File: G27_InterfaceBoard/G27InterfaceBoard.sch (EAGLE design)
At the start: 24 parts, among them IC1 LMV321M5, J1 Pedal, J2 Shifter, J3 Steering, U1 LMV324

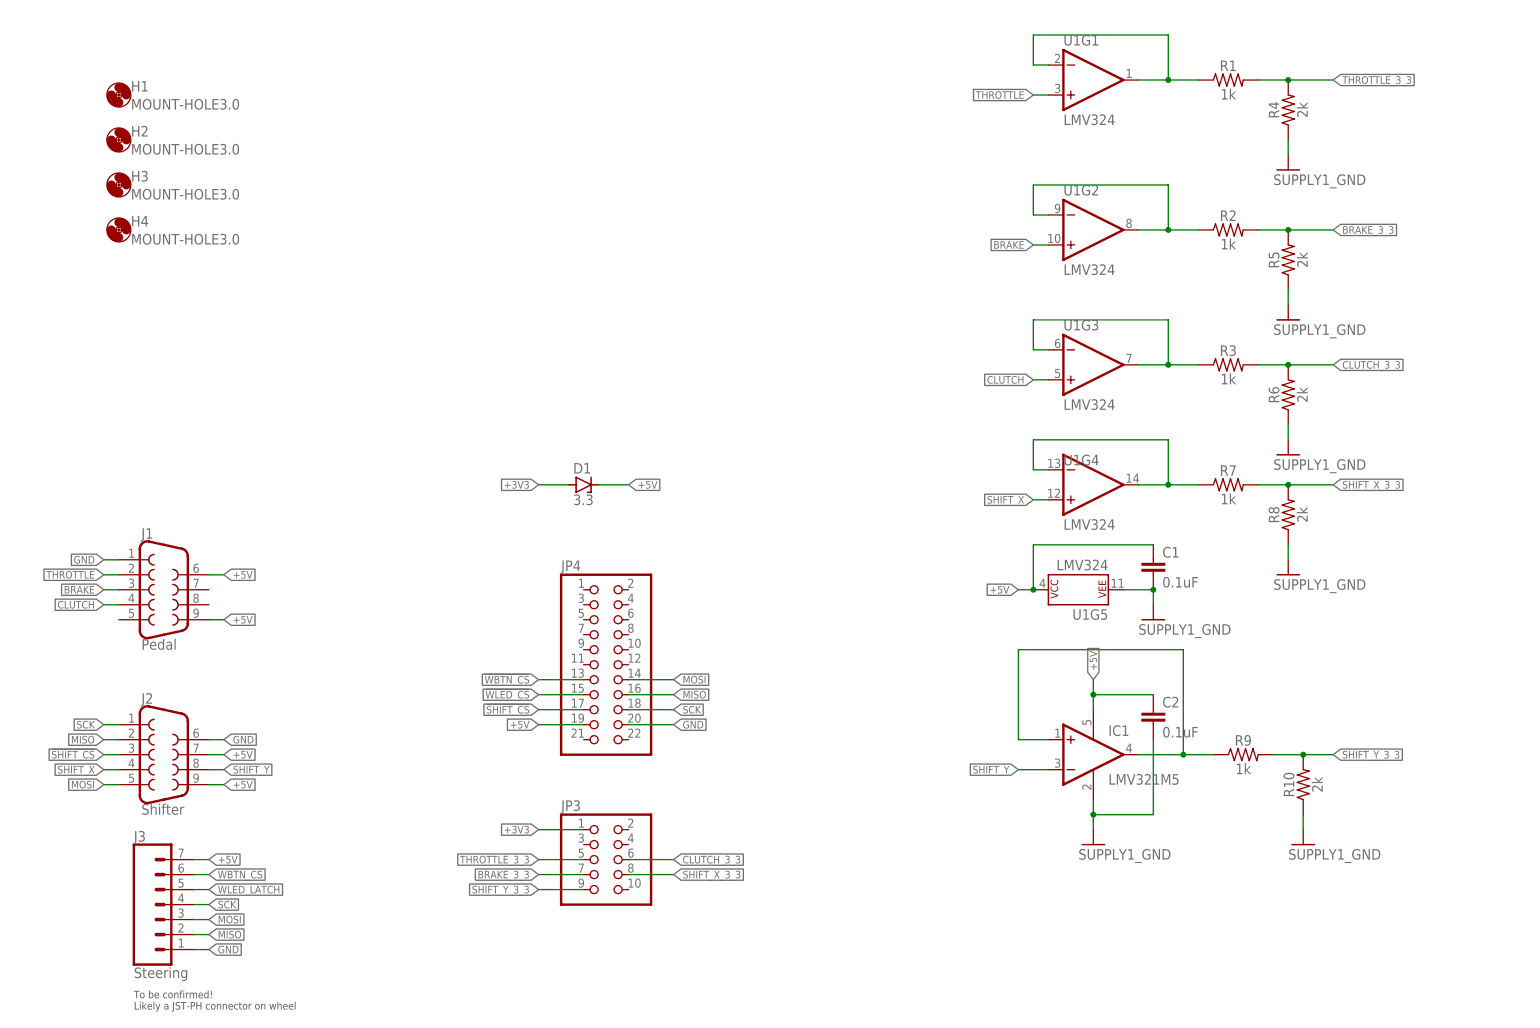
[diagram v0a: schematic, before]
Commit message: Modfications to board based on testing.
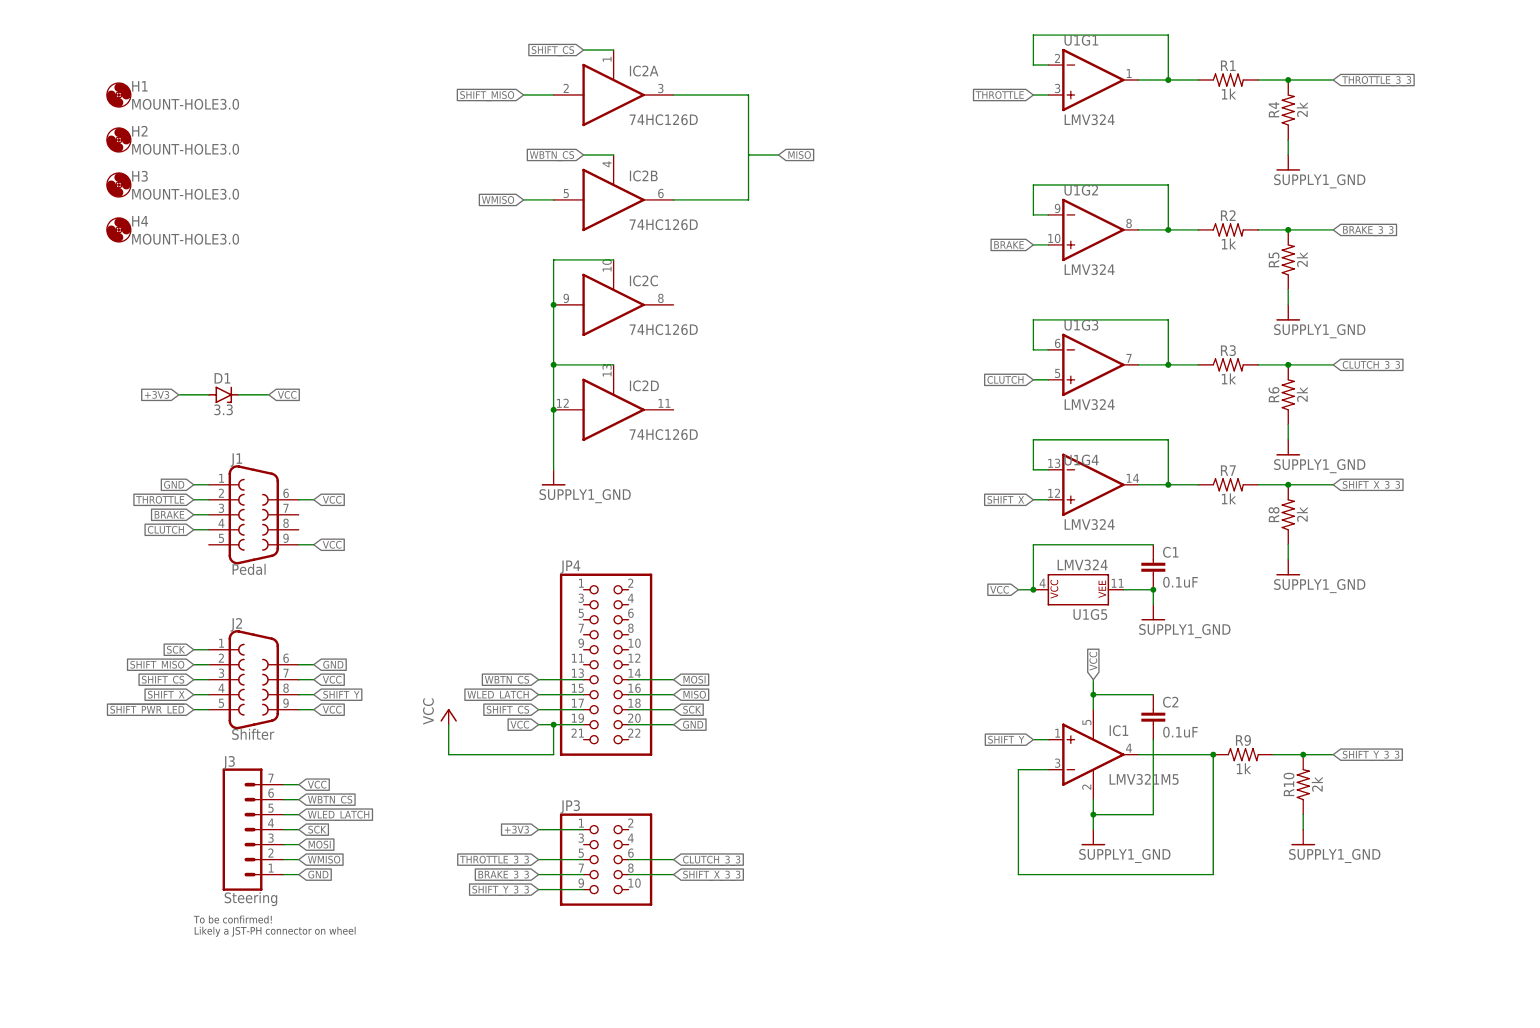
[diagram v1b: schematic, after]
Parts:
- added IC2: 74HC126D, 74xx-eu:74HC126D
- D1: SPICEPREFIX (none) -> D
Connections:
- net +5V renamed VCC
- removed net !SHIFT_CS: J2.3, JP4.17
- removed net !WBTN_CS: JP4.13
- removed net !WLED_CS: JP4.15
- removed net N$4: C2.2, IC1.V-
- new net !SHIFT_PWR_LED: J2.5
- new net SHIFT_CS: IC2A.OE, J2.3, JP4.17
- new net SHIFT_MISO: IC2A.I, J2.2
- new net WMISO: IC2B.I, J3.2
- net GND: now also C2.2, IC1.V-, IC2C.I, IC2C.OE, IC2D.I, IC2D.OE
- net MISO: now also IC2A.O, IC2B.O; no longer J2.2, J3.2
- net MOSI: no longer J2.5
- net N$3: now also IC1.-IN; no longer IC1.+IN
- net SHIFT_Y: now also IC1.+IN; no longer IC1.-IN
- net WBTN_CS: now also IC2B.OE, JP4.13
- net WLED_LATCH: now also JP4.15
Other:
- moved on the sheet: D1, J1, J2, J3

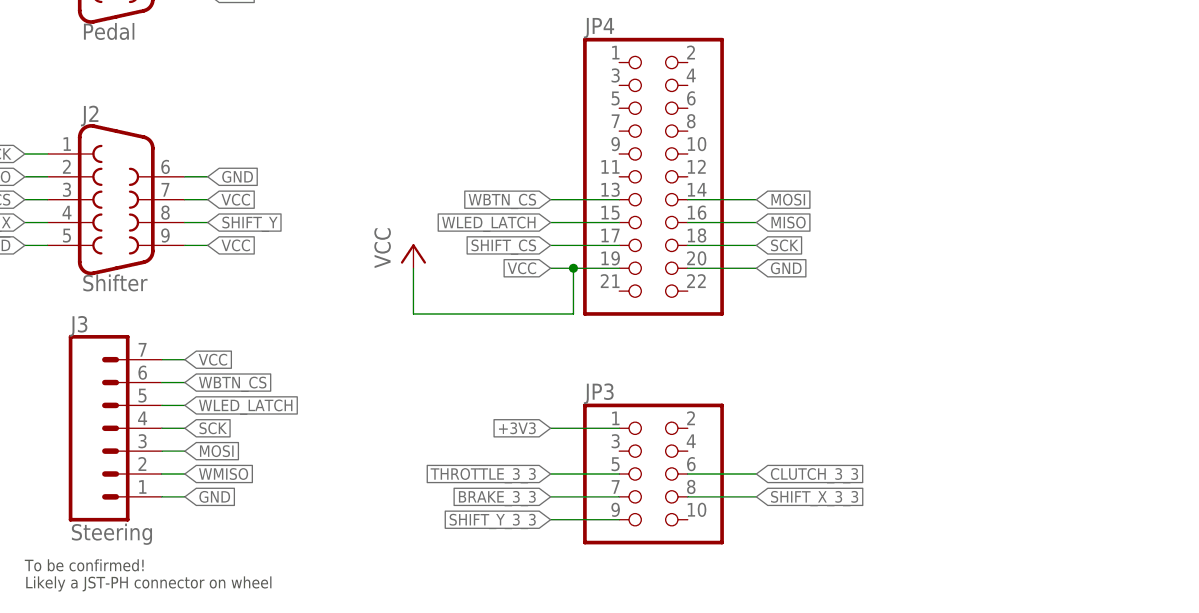
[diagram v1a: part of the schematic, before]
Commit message: Add some termination resistors to the SPI lines.
A breadboarded version of this is now working with the G27 shifter
and wheel simulataneously. LED control is not yet tested.
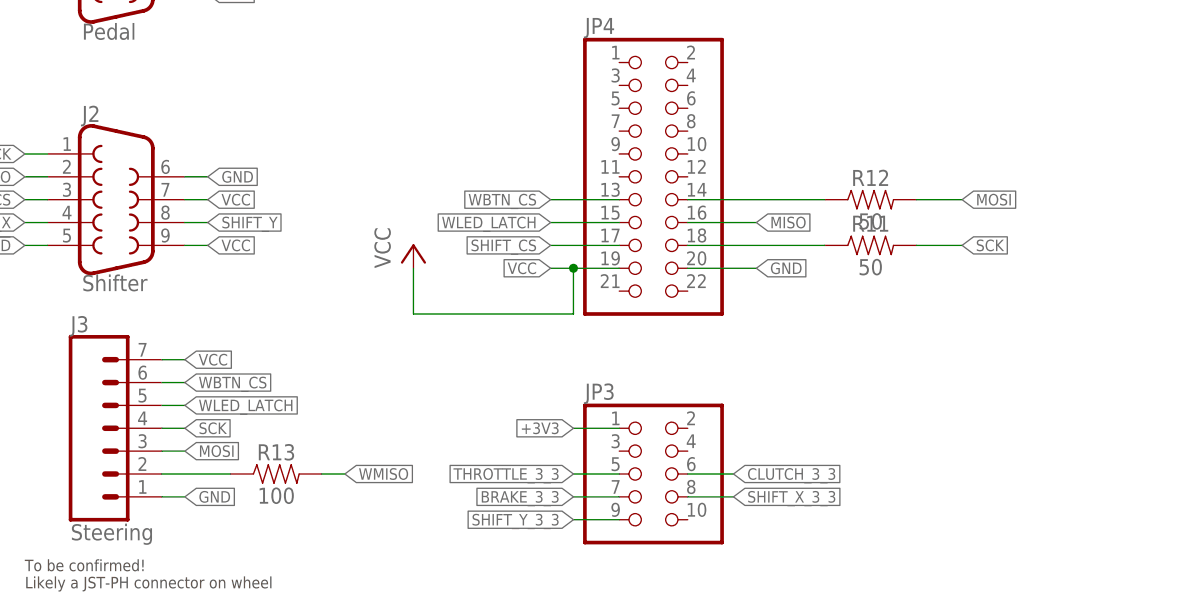
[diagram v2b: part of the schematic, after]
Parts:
- added R11, R12: 50, SparkFun-Resistors:RESISTOR0603
- added R13: 100, SparkFun-Resistors:RESISTOR0603
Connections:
- new net N$4: JP4.18, R11.1
- new net N$7: JP4.14, R12.1
- new net N$8: J3.2, R13.1
- net MOSI: now also R12.2; no longer JP4.14
- net SCK: now also R11.2; no longer JP4.18
- net WMISO: now also R13.2; no longer J3.2
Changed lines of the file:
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@@
 <part name="P+1" library="supply1" library_urn="urn:adsk.eagle:library:371" deviceset="VCC" device=""/>
 <part name="GND8" library="stm_board_f407" deviceset="SUPPLY1_GND" device=""/>
+<part name="R11" library="SparkFun-Resistors" library_urn="urn:adsk.eagle:library:532" deviceset="RESISTOR" device="0603" package3d_urn="urn:adsk.eagle:package:39650/1" value="50"/>
+<part name="R12" library="SparkFun-Resistors" library_urn="urn:adsk.eagle:library:532" deviceset="RESISTOR" device="0603" package3d_urn="urn:adsk.eagle:package:39650/1" value="50"/>
+<part name="R13" library="SparkFun-Resistors" library_urn="urn:adsk.eagle:library:532" deviceset="RESISTOR" device="0603" package3d_urn="urn:adsk.eagle:package:39650/1" value="100"/>
 </parts>
 <sheets>
@@
 <instance part="GND8" gate="1" x="91.44" y="93.98" smashed="yes">
 <attribute name="VALUE" x="88.9" y="91.44" size="1.778" layer="96"/>
+</instance>
+<instance part="R11" gate="G$1" x="124.46" y="55.88" smashed="yes">
+<attribute name="NAME" x="124.46" y="57.404" size="1.778" layer="95" font="vector" align="bottom-center"/>
+<attribute name="VALUE" x="124.46" y="54.356" size="1.778" layer="96" font="vector" align="top-center"/>
+</instance>
+<instance part="R12" gate="G$1" x="124.46" y="60.96" smashed="yes">
+<attribute name="NAME" x="124.46" y="62.484" size="1.778" layer="95" font="vector" align="bottom-center"/>
+<attribute name="VALUE" x="124.46" y="59.436" size="1.778" layer="96" font="vector" align="top-center"/>
+</instance>
+<instance part="R13" gate="G$1" x="58.42" y="30.48" smashed="yes">
+<attribute name="NAME" x="58.42" y="32.004" size="1.778" layer="95" font="vector" align="bottom-center"/>
+<attribute name="VALUE" x="58.42" y="28.956" size="1.778" layer="96" font="vector" align="top-center"/>
 </instance>
 </instances>
@@
 </segment>
 <segment>
-<pinref part="JP4" gate="A" pin="18"/>
-<wire x1="104.14" y1="55.88" x2="111.76" y2="55.88" width="0.1524" layer="91"/>
-<label x="111.76" y="55.88" size="1.27" layer="95" xref="yes"/>
-</segment>
-<segment>
 <pinref part="J3" gate="G$1" pin="4"/>
 <wire x1="45.72" y1="35.56" x2="48.26" y2="35.56" width="0.1524" layer="91"/>
 <label x="48.26" y="35.56" size="1.27" layer="95" xref="yes"/>
+</segment>
+<segment>
+<pinref part="R11" gate="G$1" pin="2"/>
+<wire x1="129.54" y1="55.88" x2="134.62" y2="55.88" width="0.1524" layer="91"/>
+<label x="134.62" y="55.88" size="1.27" layer="95" xref="yes"/>
 </segment>
 </net>
@@
 <net name="MOSI" class="0">
 <segment>
-<pinref part="JP4" gate="A" pin="14"/>
-<wire x1="104.14" y1="60.96" x2="111.76" y2="60.96" width="0.1524" layer="91"/>
-<label x="111.76" y="60.96" size="1.27" layer="95" xref="yes"/>
-</segment>
-<segment>
 <pinref part="J3" gate="G$1" pin="3"/>
 <wire x1="45.72" y1="33.02" x2="48.26" y2="33.02" width="0.1524" layer="91"/>
 <label x="48.26" y="33.02" size="1.27" layer="95" xref="yes"/>
+</segment>
+<segment>
+<pinref part="R12" gate="G$1" pin="2"/>
+<wire x1="129.54" y1="60.96" x2="134.62" y2="60.96" width="0.1524" layer="91"/>
+<label x="134.62" y="60.96" size="1.27" layer="95" xref="yes"/>
 </segment>
 </net>
@@
 <segment>
 <pinref part="JP3" gate="A" pin="5"/>
-<wire x1="96.52" y1="30.48" x2="88.9" y2="30.48" width="0.1524" layer="91"/>
-<label x="88.9" y="30.48" size="1.27" layer="95" rot="R180" xref="yes"/>
+<wire x1="96.52" y1="30.48" x2="91.44" y2="30.48" width="0.1524" layer="91"/>
+<label x="91.44" y="30.48" size="1.27" layer="95" rot="R180" xref="yes"/>
 </segment>
 </net>
@@
 <segment>
 <pinref part="JP3" gate="A" pin="7"/>
-<wire x1="96.52" y1="27.94" x2="88.9" y2="27.94" width="0.1524" layer="91"/>
-<label x="88.9" y="27.94" size="1.27" layer="95" rot="R180" xref="yes"/>
+<wire x1="96.52" y1="27.94" x2="91.44" y2="27.94" width="0.1524" layer="91"/>
+<label x="91.44" y="27.94" size="1.27" layer="95" rot="R180" xref="yes"/>
 </segment>
 </net>
@@
 <segment>
 <pinref part="JP3" gate="A" pin="6"/>
-<wire x1="104.14" y1="30.48" x2="111.76" y2="30.48" width="0.1524" layer="91"/>
-<label x="111.76" y="30.48" size="1.27" layer="95" xref="yes"/>
+<wire x1="104.14" y1="30.48" x2="109.22" y2="30.48" width="0.1524" layer="91"/>
+<label x="109.22" y="30.48" size="1.27" layer="95" xref="yes"/>
 </segment>
 </net>
@@
 <segment>
 <pinref part="JP3" gate="A" pin="1"/>
-<wire x1="96.52" y1="35.56" x2="88.9" y2="35.56" width="0.1524" layer="91"/>
-<label x="88.9" y="35.56" size="1.27" layer="95" rot="R180" xref="yes"/>
+<wire x1="96.52" y1="35.56" x2="91.44" y2="35.56" width="0.1524" layer="91"/>
+<label x="91.44" y="35.56" size="1.27" layer="95" rot="R180" xref="yes"/>
 </segment>
 <segment>
@@
 <segment>
 <pinref part="JP3" gate="A" pin="8"/>
-<wire x1="104.14" y1="27.94" x2="111.76" y2="27.94" width="0.1524" layer="91"/>
-<label x="111.76" y="27.94" size="1.27" layer="95" xref="yes"/>
+<wire x1="104.14" y1="27.94" x2="109.22" y2="27.94" width="0.1524" layer="91"/>
+<label x="109.22" y="27.94" size="1.27" layer="95" xref="yes"/>
 </segment>
 </net>
@@
 <segment>
 <pinref part="JP3" gate="A" pin="9"/>
-<wire x1="96.52" y1="25.4" x2="88.9" y2="25.4" width="0.1524" layer="91"/>
-<label x="88.9" y="25.4" size="1.27" layer="95" rot="R180" xref="yes"/>
+<wire x1="96.52" y1="25.4" x2="91.44" y2="25.4" width="0.1524" layer="91"/>
+<label x="91.44" y="25.4" size="1.27" layer="95" rot="R180" xref="yes"/>
 </segment>
 </net>
@@
 <net name="WMISO" class="0">
 <segment>
-<pinref part="J3" gate="G$1" pin="2"/>
-<wire x1="45.72" y1="30.48" x2="48.26" y2="30.48" width="0.1524" layer="91"/>
-<label x="48.26" y="30.48" size="1.27" layer="95" xref="yes"/>
-</segment>
-<segment>
 <pinref part="IC2" gate="B" pin="I"/>
 <wire x1="91.44" y1="142.24" x2="86.36" y2="142.24" width="0.1524" layer="91"/>
 <label x="86.36" y="142.24" size="1.27" layer="95" rot="R180" xref="yes"/>
 </segment>
+<segment>
+<pinref part="R13" gate="G$1" pin="2"/>
+<wire x1="63.5" y1="30.48" x2="66.04" y2="30.48" width="0.1524" layer="91"/>
+<label x="66.04" y="30.48" size="1.27" layer="95" xref="yes"/>
+</segment>
 </net>
 <net name="SHIFT_MISO" class="0">
@@
 </segment>
 </net>
+<net name="N$4" class="0">
+<segment>
+<pinref part="JP4" gate="A" pin="18"/>
+<pinref part="R11" gate="G$1" pin="1"/>
+<wire x1="104.14" y1="55.88" x2="119.38" y2="55.88" width="0.1524" layer="91"/>
+</segment>
+</net>
+<net name="N$7" class="0">
+<segment>
+<pinref part="JP4" gate="A" pin="14"/>
+<wire x1="104.14" y1="60.96" x2="119.38" y2="60.96" width="0.1524" layer="91"/>
+<pinref part="R12" gate="G$1" pin="1"/>
+</segment>
+</net>
+<net name="N$8" class="0">
+<segment>
+<pinref part="J3" gate="G$1" pin="2"/>
+<pinref part="R13" gate="G$1" pin="1"/>
+<wire x1="45.72" y1="30.48" x2="53.34" y2="30.48" width="0.1524" layer="91"/>
+</segment>
+</net>

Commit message: G27InterfaceBoard v1.0 as ordered.
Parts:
- removed J3: Steering, SparkFun-Connectors:CONN_07LONGPADS
- removed JP4: (no value), stm_board_f407:PINHEAD_PINHD-2X11
- removed R11, R12: 50, SparkFun-Resistors:RESISTOR0603
- added C3, C4: 0.1uF, resistor:C-EUC0805
- added C5, C6: 1.0uF, resistor:C-EUC0805
- added R14: 100, resistor:R-EU_R0603
- added R15: 51, resistor:R-EU_R0603
- added SPI2: (no value), pinhead:PINHD-1X9
- added WHEEL: RJ45, SparkFun-Connectors:RJ45-8
- D1: value 3.3 -> 3
- H1, H2, H3, H4: value MOUNT-HOLE3.0 -> MOUNT-PAD-ROUND3.0; device holes:MOUNT-HOLE3.0 -> holes:MOUNT-PAD-ROUND3.0
- R1, R2, R3, R7, R9: value 1k -> 1.2k; device SparkFun-Resistors:RESISTOR0603 -> resistor:R-EU_R0603
- R10, R4, R5, R6, R8: value 2k -> 7.5k; device SparkFun-Resistors:RESISTOR0603 -> resistor:R-EU_R0603
- R13: value 100 -> 51; device SparkFun-Resistors:RESISTOR0603 -> resistor:R-EU_R0603
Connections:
- removed net N$4: JP4.18, R11.1
- removed net N$7: JP4.14, R12.1
- new net N$10: R15.1, SPI2.6
- new net N$9: R14.1, WHEEL.4
- new net SCLK: WHEEL.7
- net +3V3: now also C4.1, C6.1, SPI2.2
- net GND: now also C3.2, C4.2, C5.2, C6.2, H1.MOUNT, H2.MOUNT, H3.MOUNT, H4.MOUNT, SPI2.1, WHEEL.2, WHEEL.8; no longer J3.1, JP4.20
- net MISO: now also SPI2.5; no longer JP4.16
- net MOSI: now also R15.2, WHEEL.5; no longer J3.3, R12.2
- net N$8: now also SPI2.4; no longer J3.2
- net SCK: now also R13.2; no longer J3.4, R11.2
- net SHIFT_CS: now also SPI2.7; no longer JP4.17
- net VCC: now also C3.1, C5.1, SPI2.9, WHEEL.1; no longer J3.7, JP4.19
- net WBTN_CS: now also SPI2.3, WHEEL.3; no longer J3.6, JP4.13
- net WLED_LATCH: now also SPI2.8, WHEEL.6; no longer J3.5, JP4.15
- net WMISO: now also R14.2; no longer R13.2
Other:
- moved on the sheet: JP3

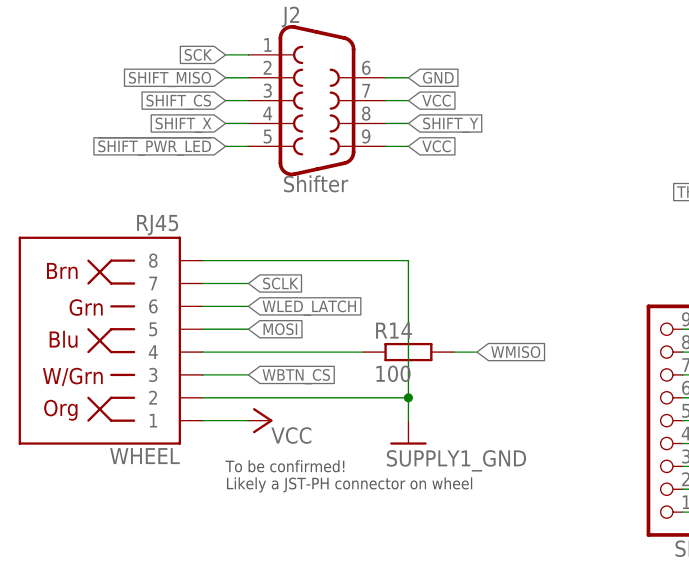
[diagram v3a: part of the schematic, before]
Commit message: Add missing trace for wheel SCK.
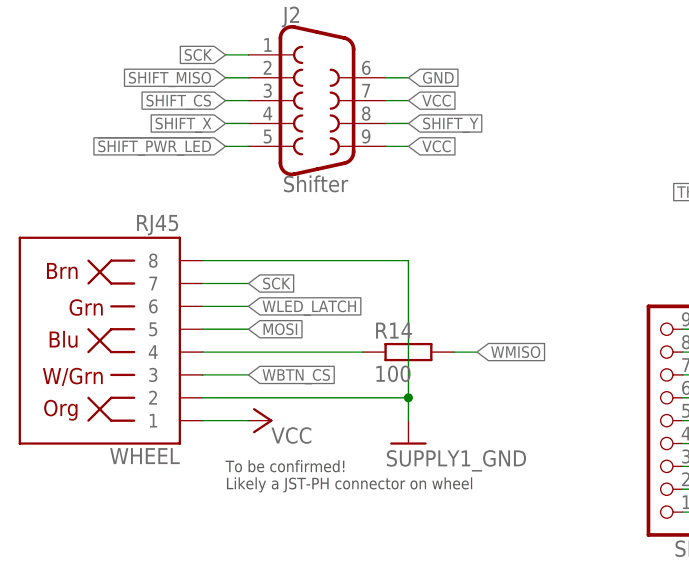
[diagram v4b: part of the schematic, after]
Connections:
- removed net SCLK: WHEEL.7
- net SCK: now also WHEEL.7
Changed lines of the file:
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@@
 <label x="114.3" y="22.86" size="1.27" layer="95" xref="yes"/>
+</segment>
+<segment>
+<pinref part="WHEEL" gate="JP1" pin="7"/>
+<wire x1="27.94" y1="40.64" x2="33.02" y2="40.64" width="0.1524" layer="91"/>
+<label x="33.02" y="40.64" size="1.27" layer="95" xref="yes"/>
 </segment>
 </net>
@@
 </segment>
 </net>
-<net name="SCLK" class="0">
-<segment>
-<pinref part="WHEEL" gate="JP1" pin="7"/>
-<wire x1="27.94" y1="40.64" x2="33.02" y2="40.64" width="0.1524" layer="91"/>
-<label x="33.02" y="40.64" size="1.27" layer="95" xref="yes"/>
-</segment>
-</net>
